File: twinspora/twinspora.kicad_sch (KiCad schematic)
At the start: 138 parts, among them J1 TYPE-C-31-M-12, J10 XY-SH1_0-4A61, J12 XY-SH1_0-3A61, J13 Conn_01x02, J5 XY-SH1_0-3A61, J6 XY-SH1_0-3A61, J7 Conn_01x02, Q1 AO3401A, SW1 SKSGPAE010, SW2 SKSGPAE010, U1 STM32G473RBTx, U13 WSD4066DN, U14 FMMT620TA, U15 BK22C07-4DP/2-0_4V(800), U16 BK22C07-4DP/2-0_4V(800), U2 SRV05-4A, U3 SRV05-4A, U4 XC6206P332MR, U5 CA-IF1044VD-Q1, X1 X322512MSB4SI

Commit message: MORE ESD
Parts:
- removed C10, C11: 0402CG200J500NT, Capacitor_SMD:C_0402_1005Metric, symbol Basic_Capacitors_Resistors:0402CG200J500NT
- added C10, C11: 0402CG300J500NT, footprints/Basic_Capacitors_Resistors:C0402, symbol Basic_Capacitors_Resistors:0402CG300J500NT
- added C56: CL10A475KO8NNNC, Capacitor_SMD:C_0603_1608Metric, symbol Basic_Capacitors_Resistors:CL10A475KO8NNNC
- added C57: CL05A105KA5NQNC, Capacitor_SMD:C_0402_1005Metric, symbol Basic_Capacitors_Resistors:CL05A105KA5NQNC
- added R37, R38: 0603WAF0000T5E, Resistor_SMD:R_0603_1608Metric, symbol Basic_Capacitors_Resistors:0603WAF0000T5E
- added U12: H5VN10B, Diode_UWRL:DFN1006-2L-BI, symbol Diode_UWRL:H5VN10B
- added U17: ACT1210D-101-2P-TL00, CMC_UWRL:FILTER-SMD_4P-L3.2-W2.5-BL_ACT1210D-101-2P-TL00, symbol CMC_UWRL:ACT1210D-101-2P-TL00
- added U18: PESD2CAN, Diode_UWRL:SOT-23-3_L2.9-W1.3-P1.90-LS2.4-BR, symbol Diode_UWRL:PESD2CAN
- added U19: SMF30CA_C19077519, Diode_UWRL:SOD-123FL_L2.7-W1.8-LS3.8-BI, symbol Diode_UWRL:SMF30CA_C19077519
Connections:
- net +5V: now also C56.2, C57.2, U12.2
- net CAN_H: now also R38.2, U17.4, U18.1; no longer U5.7 (CANH)
- net CAN_L: now also R37.2, U17.3, U18.2; no longer U5.6 (CANL)
- net GND: now also C10.2, C11.1, C56.1, C57.1, U12.1, U18.3, U19.2 (A)
- net RCC_OSC_IN: now also C10.1
- net RCC_OSC_OUT: now also C11.2
- net VCC: now also U19.1 (C)
- new net: R37.1, U17.2, U5.6 (CANL)
- new net: R38.1, U17.1, U5.7 (CANH)
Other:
- moved on the sheet: C22, C23, C24, C49, C50, C51, C52, C53, D1, J1, J12, J5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

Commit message: split terminatino for can
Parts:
- added C30: CL05B103KB5NNNC, Capacitor_SMD:C_0402_1005Metric, symbol Basic_Capacitors_Resistors:CL05B103KB5NNNC
- added R27, R28: 0402WGF604JTCE, Resistor_SMD:R_0402_1005Metric, symbol Basic_Capacitors_Resistors:0402WGF604JTCE
- C11: renamed from C10; footprint footprints/Basic_Capacitors_Resistors:C0402 -> Capacitor_SMD:C_0402_1005Metric
- C18: renamed from C11; footprint footprints/Basic_Capacitors_Resistors:C0402 -> Capacitor_SMD:C_0402_1005Metric
- R21: renamed from R17; now not fitted
- renumbered C50 to C1, C16 to C10, C18 to C12, C15 to C13, C56 to C14, C17 to C15, C24 to C16, C19 to C17, C23 to C19, C49 to C2, C1 to C20, C2 to C21, C3 to C22, C4 to C23, C5 to C24, C6 to C25, C7 to C26, C8 to C27, C9 to C28, C13 to C29, C12 to C3, C22 to C4, C57 to C5, C53 to C6, C52 to C7, C51 to C8, C14 to C9, D4 to D1, D1 to D2, H4 to H10, H8 to H11, H16 to H12, H5 to H2, H13 to H3, H2 to H4, H6 to H5, H14 to H6, H3 to H7, H7 to H8, H15 to H9, J12 to J1, J1 to J2, J11 to J3, J13 to J4, J10 to J5, J7 to J6, J5 to J7, J6 to J8, LED3 to LED1, LED1 to LED2, LED2 to LED3, R32 to R1, R15 to R10, R16 to R11, R7 to R12, R8 to R13, R9 to R14, R24 to R15, R25 to R16, R10 to R17, R23 to R18, R11 to R19, R13 to R2, R12 to R20, R18 to R22, R38 to R23, R37 to R24, R5 to R25, R6 to R26, R14 to R3, R33 to R4, R34 to R5, R3 to R6, R4 to R7, R1 to R8, R2 to R9, SW2 to SW1, SW1 to SW2, U15 to U1, U3 to U10, U5 to U11, U17 to U12, U18 to U13, U16 to U2, U14 to U3, U13 to U4, U19 to U5, U2 to U6, U1 to U7, U12 to U8, U4 to U9
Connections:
- net CAN_H: now also R28.2
- net GND: now also C30.1
- net at J6.2 (Pin_2), R21.1: now also R27.1
- new net: C30.2, R27.2, R28.1
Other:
- note added: "CAN Termination — regular & split"
- moved on the sheet: TP1, TP10, TP11, TP12, TP13, TP14, TP15, TP16, TP17, TP18, TP19, TP2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

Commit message: rear silkscreen
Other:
- moved on the sheet: C20, C21, C22, C23, C24, C25, C26, C27, C28, C29, R25, R26

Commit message: fin
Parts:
- removed J4, J6: Conn_01x02, symbol Connector_Generic:Conn_01x02
- added J13: Conn_01x04, Connector_PinHeader_2.54mm:PinHeader_1x04_P2.54mm_Vertical, symbol Connector_Generic:Conn_01x04
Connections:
- net +3.3V: now also J13.4 (Pin_4)
- net CAN_L: now also J13.2 (Pin_2)
- net at R21.1, R27.1: now also J13.1 (Pin_1)
- net at R18.2: now also J13.3 (Pin_3)
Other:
- moved on the sheet: C20, C21, C22, C23, C24, C25, C26, C27, C28, C30, R18, R21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

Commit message: ferrite bead
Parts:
- added L3: GZ1608D601TF, Inductor_SMD:L_0603_1608Metric, symbol Inductor__C:GZ1608D601TF
- added R39: 0603WAF0000T5E, Resistor_SMD:R_0603_1608Metric, symbol Basic_Capacitors_Resistors:0603WAF0000T5E
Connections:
- net +3.3V: now also L3.2, R39.2; no longer C25.1, C26.1, C27.1, C28.1, U7.28 (VREF+), U7.29 (VDDA)
- new net VDDA_DECOUPLE: C25.1, C26.1, C27.1, C28.1, L3.1, R39.1, U7.28 (VREF+), U7.29 (VDDA)
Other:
- moved on the sheet: C20, C21, C22, C23, C24, C25, C26, C27, C28, C29, R25, R26

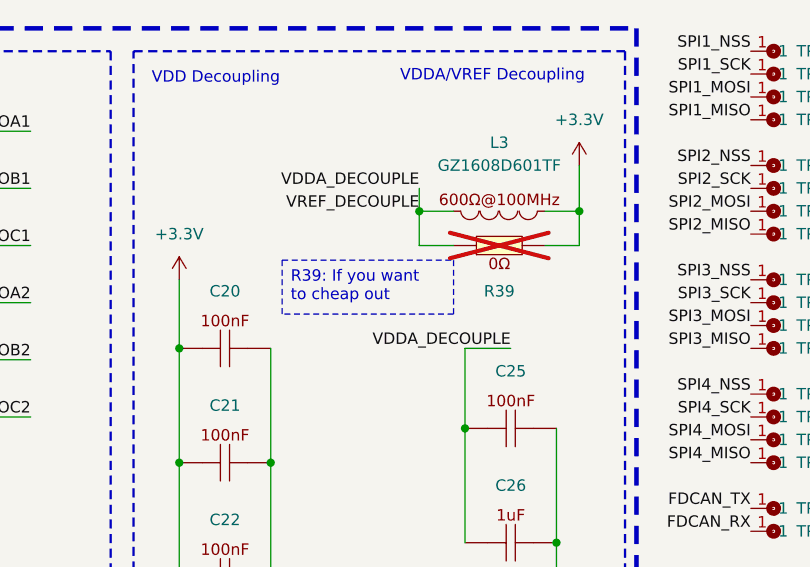
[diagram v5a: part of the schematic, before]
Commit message: fix silkscreen
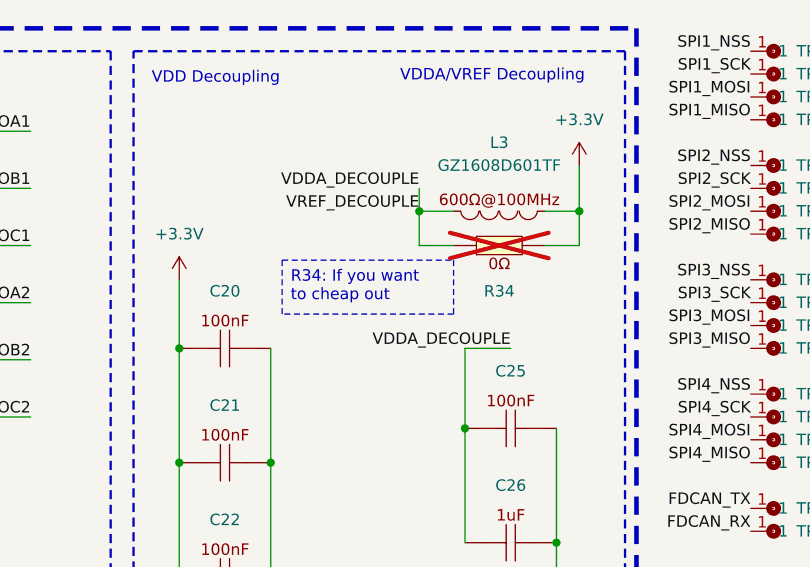
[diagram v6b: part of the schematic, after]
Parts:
- renumbered R39 to R34
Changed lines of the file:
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@@
 		)
 	)
-	(text_box "R39: If you want to cheap out"
+	(text_box "R34: If you want to cheap out"
 		(exclude_from_sim no)
 		(at 341.63 103.2271 0)
@@
 		(in_pos_files yes)
 		(dnp yes)
-		(property "Reference" "R39"
+		(property "Reference" "R34"
 			(at 365.76 106.68 0)
 			(show_name no)
@@
 			(project "twinspora"
 				(path "/64e594d2-0aaa-4fb1-a4b5-254d61e53018"
-					(reference "R39")
+					(reference "R34")
 					(unit 1)
 				)

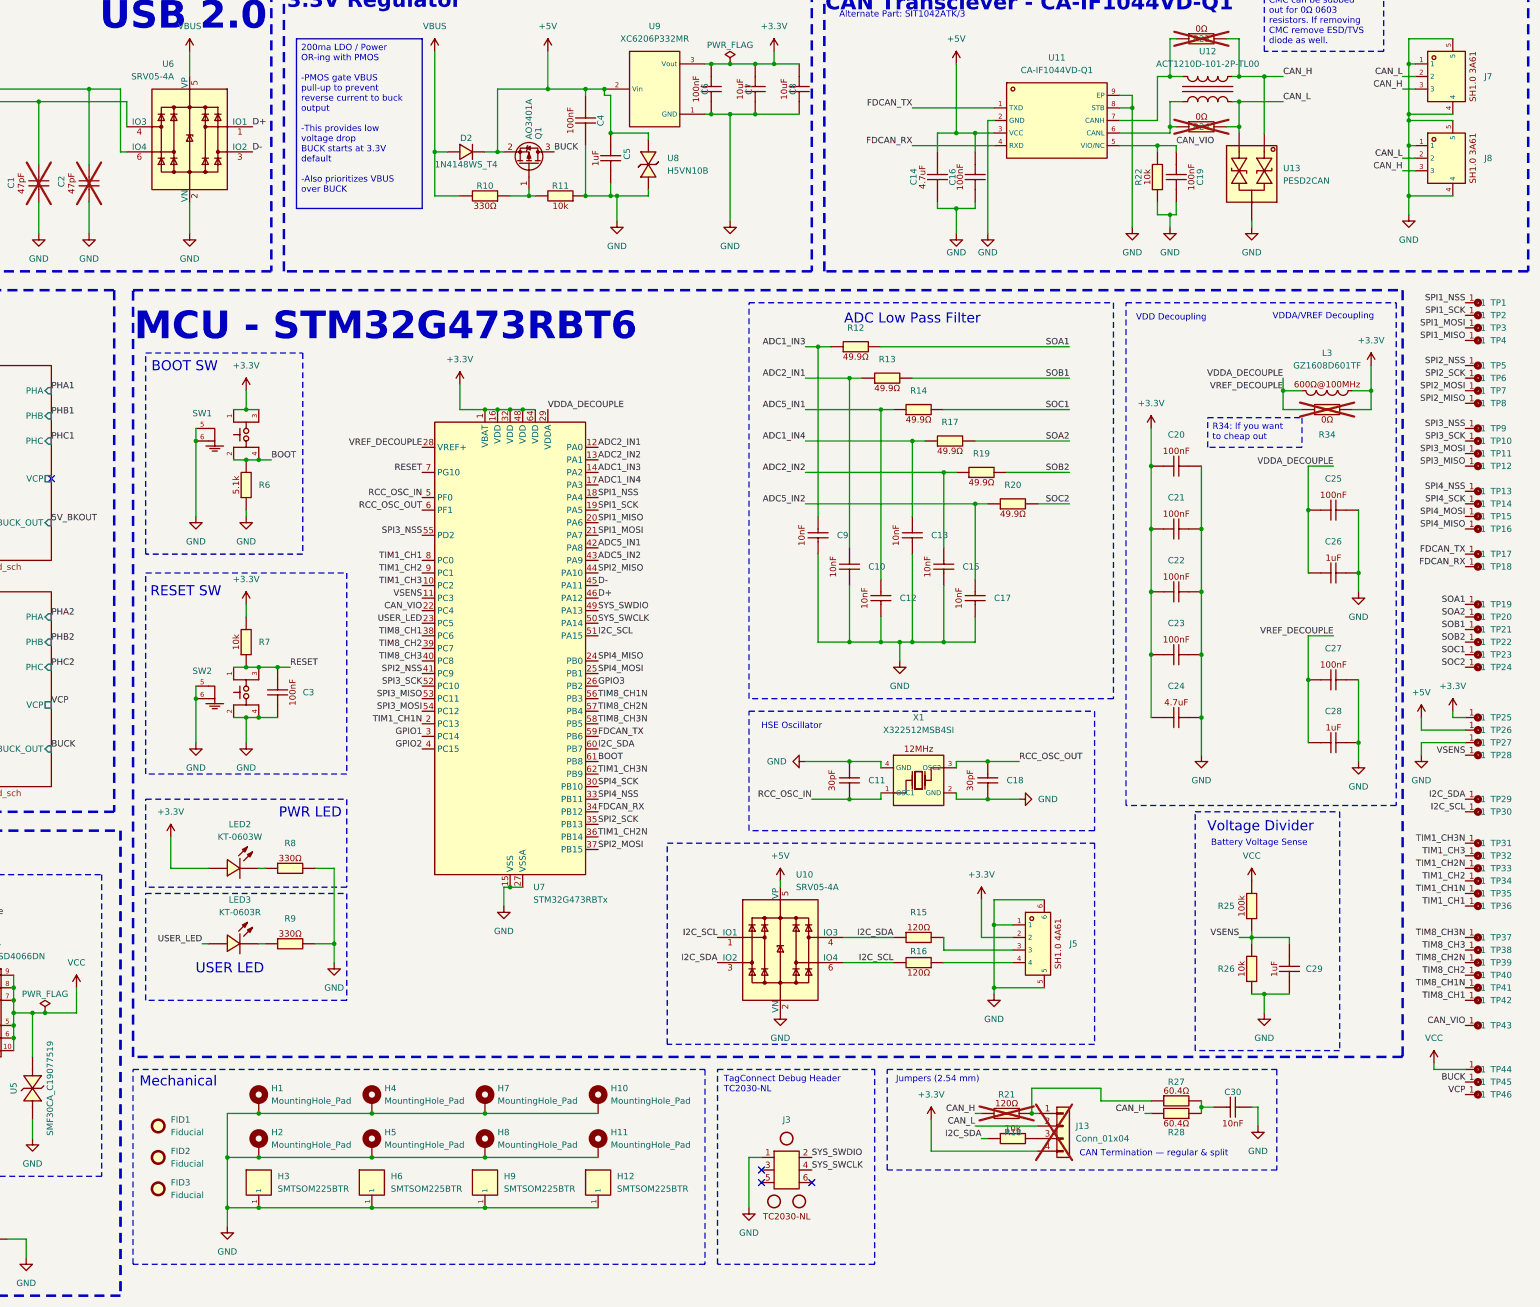
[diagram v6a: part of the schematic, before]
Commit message: forgot the other i2c pullup
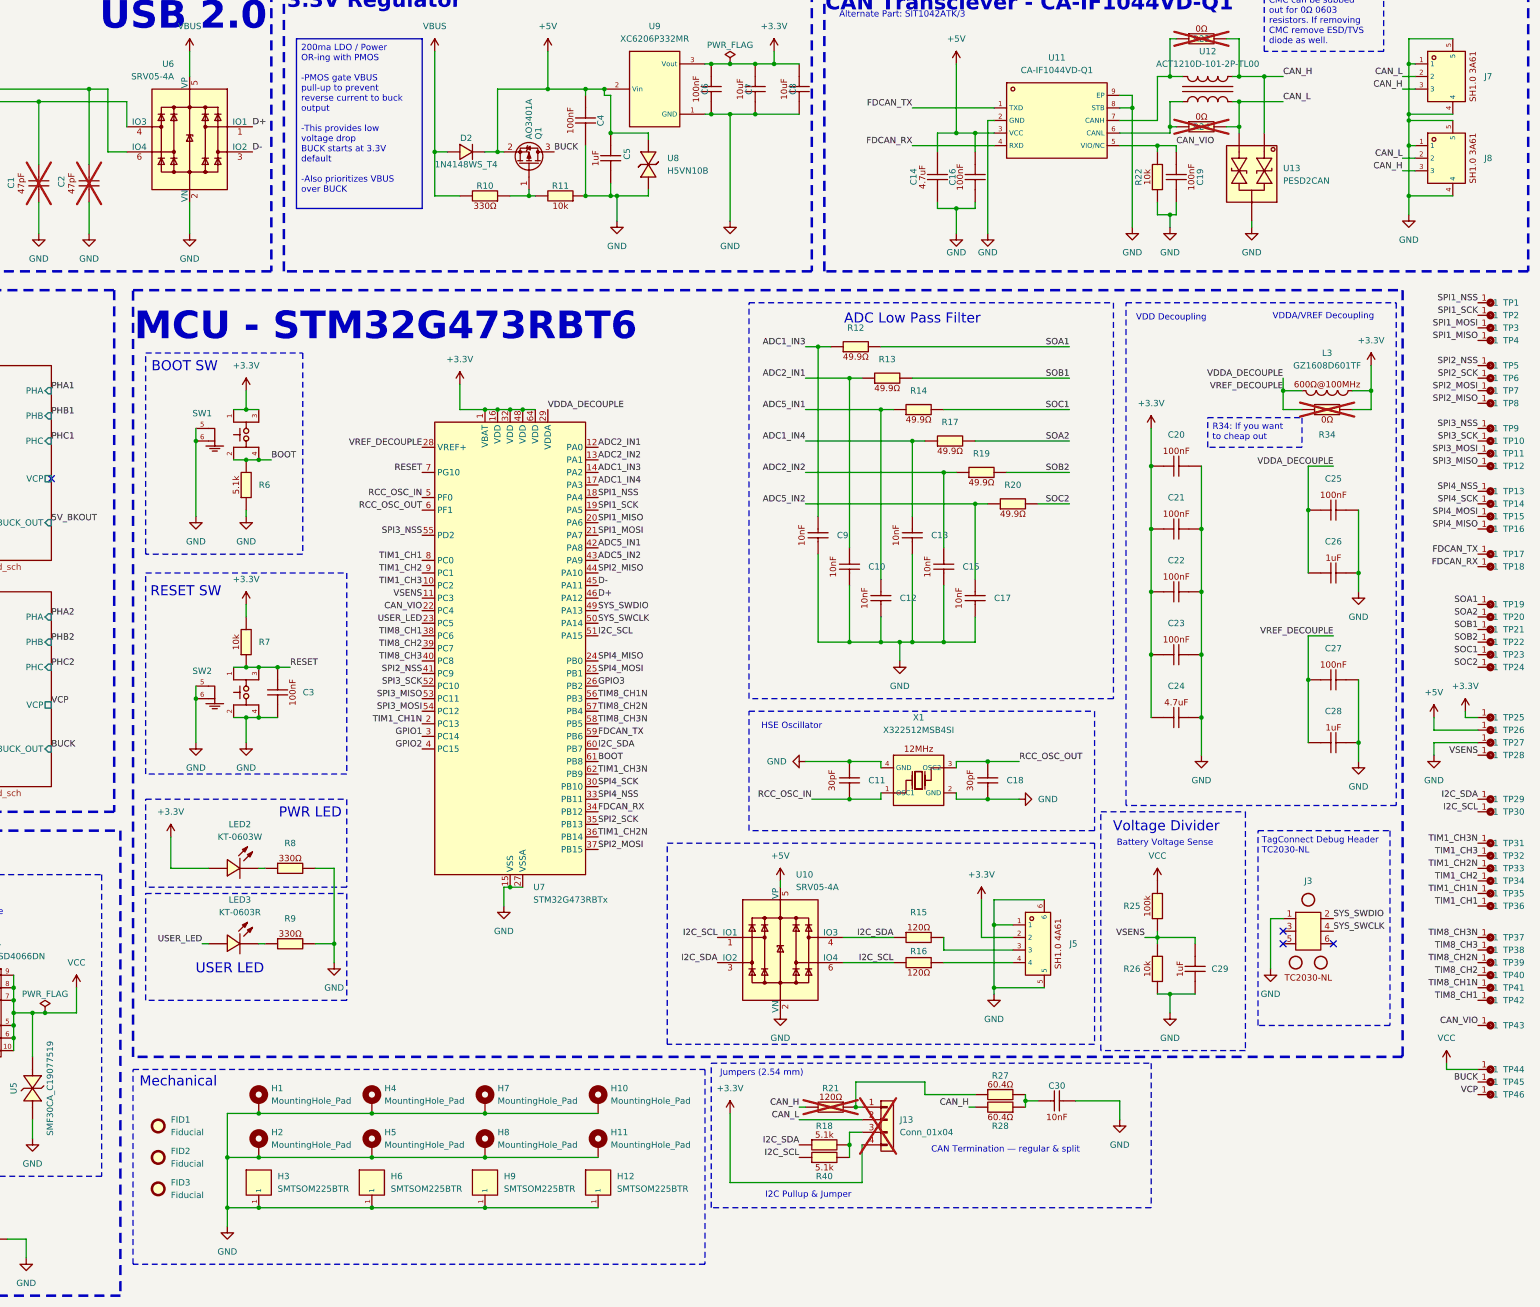
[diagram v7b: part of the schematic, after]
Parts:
- removed R18: 0402WGF1002TCE, Resistor_SMD:R_0402_1005Metric, symbol Basic_Capacitors_Resistors:0402WGF1002TCE
- added R18, R40: 0402WGF5101TCE, Resistor_SMD:R_0402_1005Metric, symbol Basic_Capacitors_Resistors:0402WGF5101TCE
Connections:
- net I2C_SCL: now also R40.1
- net I2C_SDA: now also R18.1
- net at J13.3 (Pin_3): now also R18.2, R40.2
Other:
- note added: "I2C Pullup & Jumper"
- moved on the sheet: C29, C30, J13, J3, R21, R25, R26, R27, R28, TP1, TP10, TP11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

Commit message: latest
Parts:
- C1, C2: symbol Basic_Capacitors_Resistors:0402CG470J500NT -> Basic_Capacitors_Resistors__C:0402CG470J500NT
- C10, C12, C13, C15, C17, C30, C9: symbol Basic_Capacitors_Resistors:CL05B103KB5NNNC -> Basic_Capacitors_Resistors__C:CL05B103KB5NNNC
- C11, C18: symbol Basic_Capacitors_Resistors:0402CG300J500NT -> Basic_Capacitors_Resistors__C:0402CG300J500NT
- C14, C24: symbol Basic_Capacitors_Resistors:CL10A475KO8NNNC -> Basic_Capacitors_Resistors__C:CL10A475KO8NNNC
- C16, C19, C20, C21, C22, C23, C25, C27, C3, C4, C6: symbol Basic_Capacitors_Resistors:CL05B104KB54PNC -> Basic_Capacitors_Resistors__C:CL05B104KB54PNC
- C26, C28, C29, C5: symbol Basic_Capacitors_Resistors:CL05A105KA5NQNC -> Basic_Capacitors_Resistors__C:CL05A105KA5NQNC
- C7, C8: symbol Basic_Capacitors_Resistors:GRM21BR61H106KE43L -> Basic_Capacitors_Resistors__C:GRM21BR61H106KE43L
- D1, D2: symbol Diode_UWRL:1N4148WS_T4 -> Diode__C:1N4148WS_T4
- H12, H3, H6, H9: footprint Mechanical:SMD_BD5.6-D3.6 -> Mechanical__C:SMD_BD5.6-D3.6; symbol Mechanical:SMTSOM225BTR -> Mechanical__C:SMTSOM225BTR
- J1, J7, J8: footprint Connector_SH1.0:CONN-SMD_3P-P1.00_XYECONN_XY-SH1.0-3A61 -> Connector_SH1.0__C:CONN-SMD_3P-P1.00_XYECONN_XY-SH1.0-3A61; symbol Connector_SH1.0:XY-SH1_0-3A61 -> Connector_SH1.0__C:XY-SH1_0-3A61
- J2: footprint Connector_USB:USB-C_SMD-TYPE-C-31-M-12_1 -> Connector_USB__C:USB-C_SMD-TYPE-C-31-M-12_1; symbol Connector_USB:TYPE-C-31-M-12 -> Connector_USB__C:TYPE-C-31-M-12
- J3: footprint Connector:Tag-Connect_TC2030-IDC-NL -> Connector:Tag-Connect_TC2030-IDC-NL_2x03_P1.27mm_Vertical; symbol Connector:TC2030-NL -> Connector:TC2030
- J5: footprint Connector_SH1.0:CONN-SMD_4P-P1.00-WT -> Connector_SH1.0__C:CONN-SMD_4P-P1.00_XYECONN_XY-SH1.0-4A61; symbol Connector_SH1.0:XY-SH1_0-4A61 -> Connector_SH1.0__C:XY-SH1_0-4A61
- LED1, LED2: footprint LED:LED0603-R-RD_WHITE -> LED__C:LED0603-R-RD_WHITE; symbol LED:KT-0603W -> LED__C:KT-0603W
- LED3: footprint LED:LED0603-RD -> LED__C:LED0603-RD; symbol LED:KT-0603R -> LED__C:KT-0603R
- R1, R11, R22, R26, R4, R7: symbol Basic_Capacitors_Resistors:0402WGF1002TCE -> Basic_Capacitors_Resistors__C:0402WGF1002TCE
- R10, R8, R9: symbol Basic_Capacitors_Resistors:0402WGF3300TCE -> Basic_Capacitors_Resistors__C:0402WGF3300TCE
- R12, R13, R14, R17, R19, R20: symbol Basic_Capacitors_Resistors:0402WGF499JTCE -> Basic_Capacitors_Resistors__C:0402WGF499JTCE
- R15, R16, R21: symbol Basic_Capacitors_Resistors:0402WGF1200TCE -> Basic_Capacitors_Resistors__C:0402WGF1200TCE
- R18, R2, R3, R40, R5, R6: symbol Basic_Capacitors_Resistors:0402WGF5101TCE -> Basic_Capacitors_Resistors__C:0402WGF5101TCE
- R23, R24, R34: symbol Basic_Capacitors_Resistors:0603WAF0000T5E -> Basic_Capacitors_Resistors__C:0603WAF0000T5E
- R25: symbol Basic_Capacitors_Resistors:0402WGF1003TCE -> Basic_Capacitors_Resistors__C:0402WGF1003TCE
- R27, R28: symbol Basic_Capacitors_Resistors:0402WGF604JTCE -> Basic_Capacitors_Resistors__C:0402WGF604JTCE
- SW1, SW2: footprint Switch_UWRL:SW-SMD_SKSGAAE010 -> Switch__C:SW-SMD_SKSGAAE010; symbol Switch_UWRL:SKSGPAE010 -> Switch__C:SKSGPAE010
- TP1, TP10, TP11, TP12, TP13, TP14, TP15, TP16, TP17, TP18, TP19, TP2, TP20, TP21, TP22, TP23, TP24, TP25, TP26, TP27, TP28, TP29, TP3, TP30, TP31, TP32, TP33, TP34, TP35, TP36, TP37, TP38, TP39, TP4, TP40, TP41, TP42, TP43, TP44, TP45, TP46, TP5, TP6, TP7, TP8, TP9: symbol Mechanical:Test_Point -> Connector:TestPoint
- U1, U2: footprint Connector_HRS_BK22:CONN-SMD_4P-P0.40_BAM04-08073-0414 -> Connector_HRS_BK22__C:CONN-SMD_4P-P0.40_BAM04-08073-0414; symbol Connector_HRS_BK22:BK22C07-4DP/2-0_4V(800) -> Connector_HRS_BK22__C:BK22C07-4DP/2-0_4V(800)
- U10, U6: footprint Diode:SOT-23-6 -> Diode__C:SOT-23-6; symbol Diode:SRV05-4 -> Diode__C:SRV05-4
- U11: footprint Interface_CAN_LIN:DFN-8_L3.0-W3.0-P0.65-BL-EP2.45 -> Interface_CAN_LIN__C:DFN-8_L3.0-W3.0-P0.65-BL-EP2.45; symbol Interface_CAN_LIN:CA-IF1044VD-Q1 -> Interface_CAN_LIN__C:CA-IF1044VD-Q1
- U12: footprint CMC_UWRL:FILTER-SMD_4P-L3.2-W2.5-BL_ACT1210D-101-2P-TL00 -> CMC__C:FILTER-SMD_4P-L3.2-W2.5-BL_ACT1210D-101-2P-TL00; symbol CMC_UWRL:ACT1210D-101-2P-TL00 -> CMC__C:ACT1210D-101-2P-TL00
- U13: footprint Diode_UWRL:SOT-23-3_L2.9-W1.3-P1.90-LS2.4-BR -> Diode__C:SOT-23-3_L2.9-W1.3-P1.90-LS2.4-BR; symbol Diode_UWRL:PESD2CAN -> Diode__C:PESD2CAN
- U3: footprint Transistor_BJT_UWRL:SOT-23-3_L2.9-W1.6-P1.90-LS2.8-BR -> Transistor_BJT__C:SOT-23-3_L2.9-W1.6-P1.90-LS2.8-BR; symbol Transistor_BJT_UWRL:FMMT620TA -> Transistor_BJT__C:FMMT620TA
- U4: footprint Transistor_FET_UWRL:DFN-8_L3.2-W3.1-P0.65-LS3.4-BL-EP -> Transistor_FET__C:DFN-8_L3.2-W3.1-P0.65-LS3.4-BL-EP; symbol Transistor_FET_UWRL:WSD4066DN -> Transistor_FET__C:WSD4066DN
- U5: footprint Diode_UWRL:SOD-123FL_L2.7-W1.8-LS3.8-BI -> Diode__C:SOD-123FL_L2.7-W1.8-LS3.8-BI; symbol Diode_UWRL:SMF30CA_C19077519 -> Diode__C:SMF30CA_C19077519
- U8: footprint Diode_UWRL:DFN1006-2L-BI -> Diode__C:DFN1006-2L-BI; symbol Diode_UWRL:H5VN10B -> Diode__C:H5VN10B
- U9: footprint Regulator_Linear:SOT-23-3_L2.9-W1.6-P1.90-LS2.8-BR -> Regulator_Linear__C:SOT-23-3_L2.9-W1.6-P1.90-LS2.8-BR; symbol Regulator_Linear:XC6206P332MR -> Regulator_Linear__C:XC6206P332MR
- X1: footprint Oscillator:X322512MSB4SI -> Oscillator__C:X322512MSB4SI; symbol Oscillator:X322512MSB4SI -> Oscillator__C:X322512MSB4SI
